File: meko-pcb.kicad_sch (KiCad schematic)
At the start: 5 parts, among them IC2 AS5600-ASOM, J1 FH34SRJ-24S-0.5SH_99_, J2 MEM2090-00-145-00-A, SW1 SW_Push, U1 ESP32-PICO-MINI-02

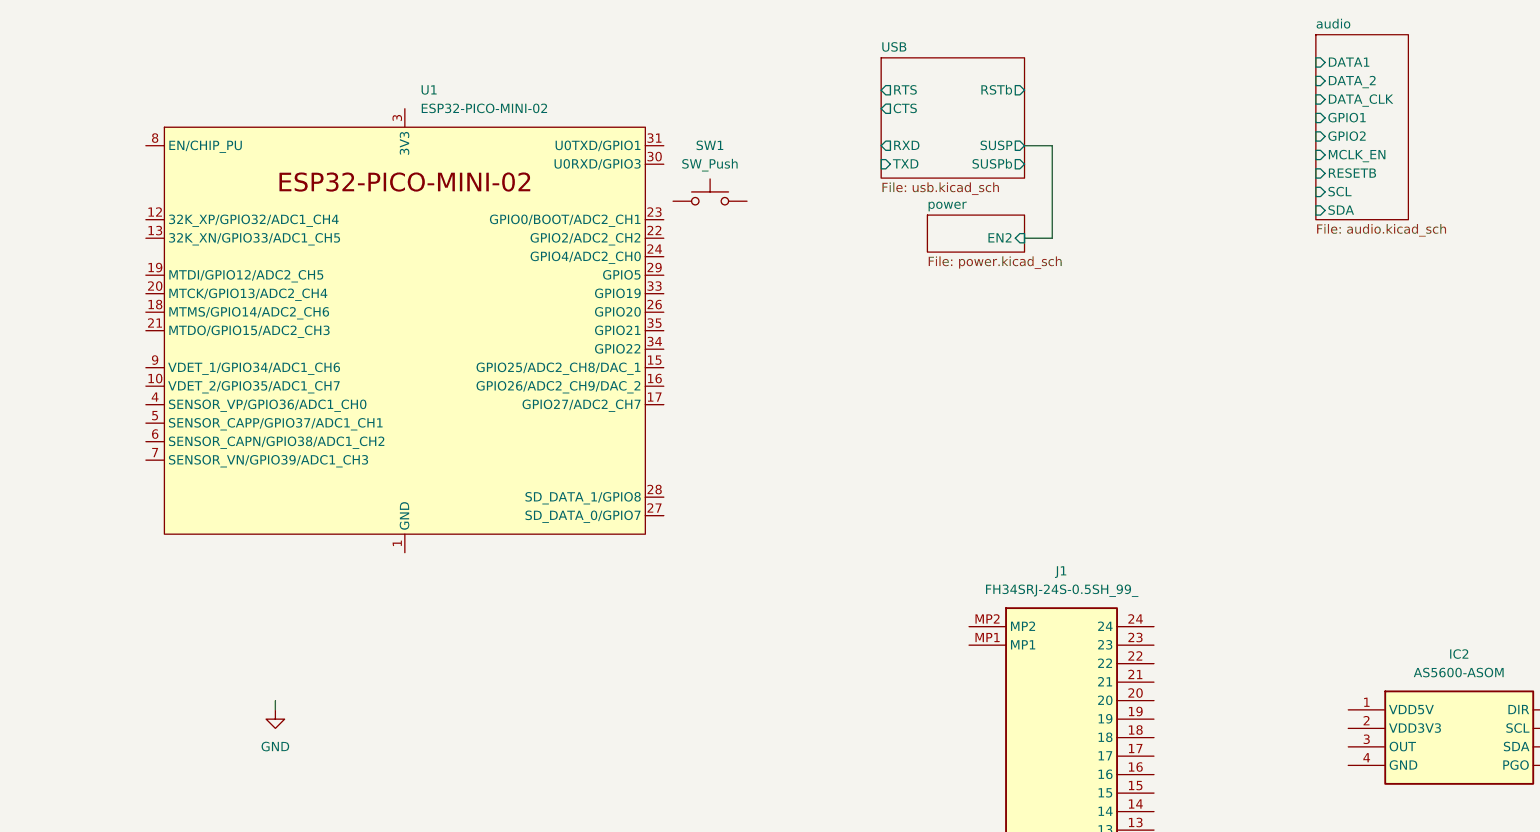
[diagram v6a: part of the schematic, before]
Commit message: made the jouranl complient, back-journaled
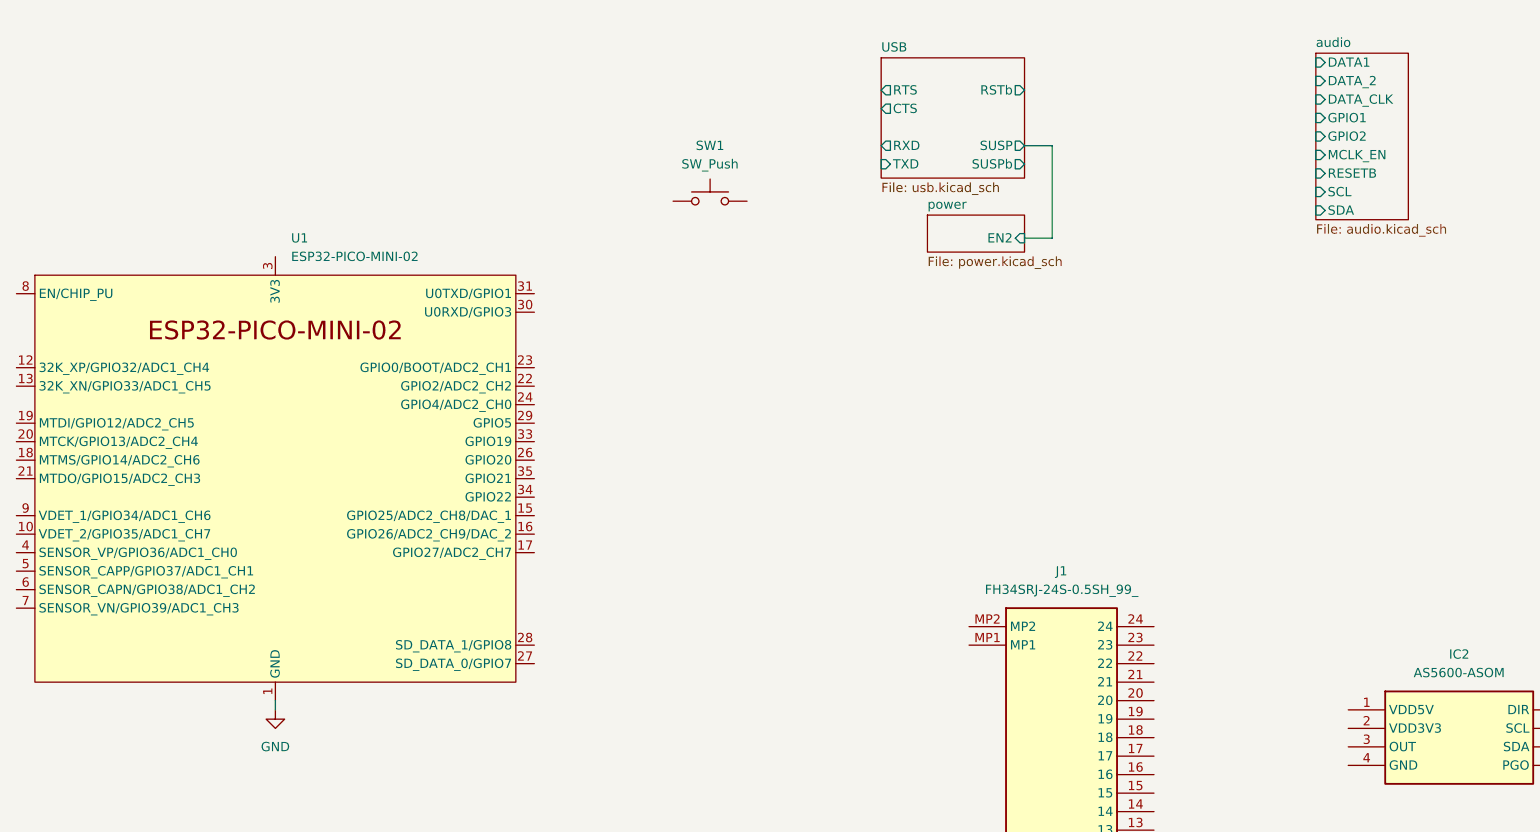
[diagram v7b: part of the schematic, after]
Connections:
- net GND: now also U1.1 (GND), U1.11 (GND), U1.14 (GND), U1.2 (GND), U1.36 (GND), U1.37 (GND), U1.38 (GND), U1.39 (GND), U1.40 (GND), U1.41 (GND), U1.42 (GND), U1.43 (GND), U1.44 (GND), U1.45 (GND), U1.46 (GND), U1.47 (GND), U1.48 (GND), U1.49 (GND), U1.50 (GND), U1.51 (GND), U1.52 (GND), U1.53 (GND)
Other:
- moved on the sheet: U1
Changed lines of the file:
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@@
 	(symbol
 		(lib_id "PCM_Espressif:ESP32-PICO-MINI-02")
-		(at 102.87 63.5 0)
+		(at 85.09 83.82 0)
 		(unit 1)
 		(exclude_from_sim no)
@@
 		(fields_autoplaced yes)
 		(property "Reference" "U1"
-			(at 105.0133 30.48 0)
+			(at 87.2333 50.8 0)
 			(effects
 				(font
@@
 		)
 		(property "Value" "ESP32-PICO-MINI-02"
-			(at 105.0133 33.02 0)
+			(at 87.2333 53.34 0)
 			(effects
 				(font
@@
 		)
 		(property "Footprint" "PCM_Espressif:ESP32-PICO-MINI-02"
-			(at 102.87 107.95 0)
+			(at 85.09 128.27 0)
 			(effects
 				(font
@@
 		)
 		(property "Datasheet" "https://www.espressif.com/sites/default/files/documentation/esp32-pico-mini-02_datasheet_en.pdf"
-			(at 102.87 110.49 0)
+			(at 85.09 130.81 0)
 			(effects
 				(font
@@
 		)
 		(property "Description" "ESP32-PICO-V3-02 MCU, SiP, 8MB Flash, 2 MB PSRAM in ESP32-MINI-format"
-			(at 102.87 63.5 0)
+			(at 85.09 83.82 0)
 			(effects
 				(font
@@
 	)
 	(sheet
-		(at 227.965 22.86)
-		(size 12.7 25.4)
+		(at 227.965 25.4)
+		(size 12.7 22.86)
 		(exclude_from_sim no)
 		(in_bom yes)
@@
 		)
 		(property "Sheetname" "audio"
-			(at 227.965 22.1484 0)
-			(effects
-				(font
+			(at 227.965 24.6884 0)
+			(effects
+				(font

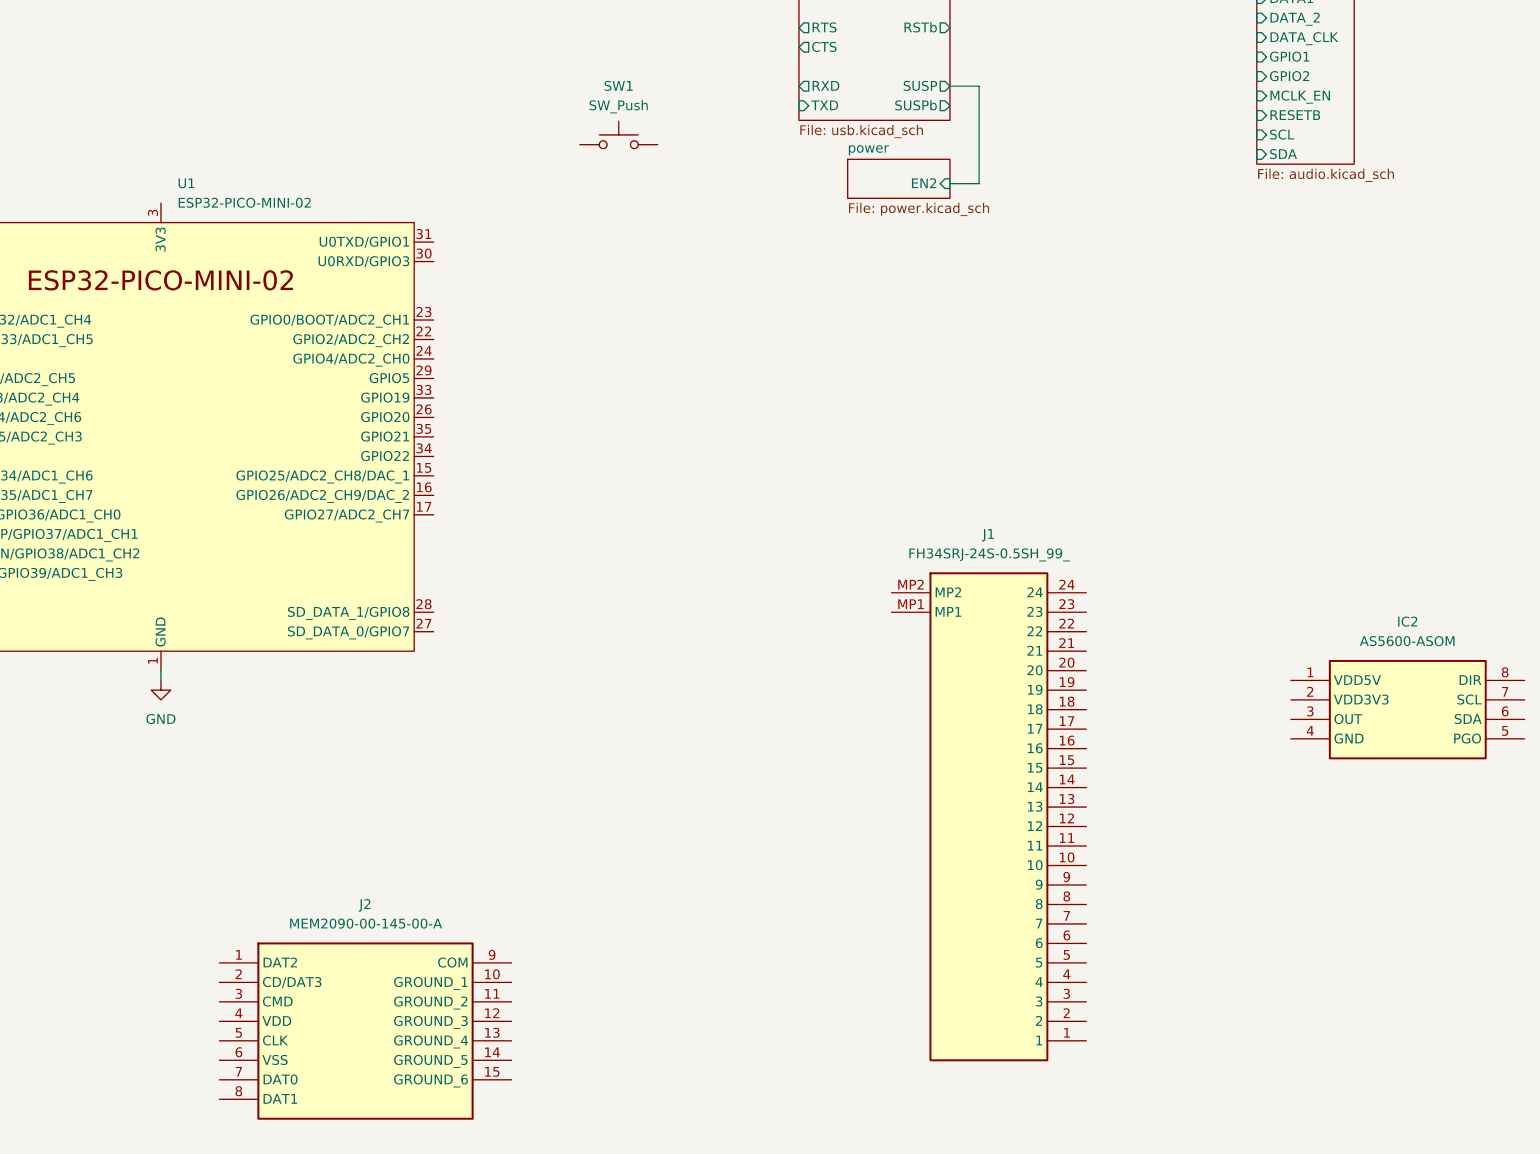
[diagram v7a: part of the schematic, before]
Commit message: re-did power with the new small LDOs and power system
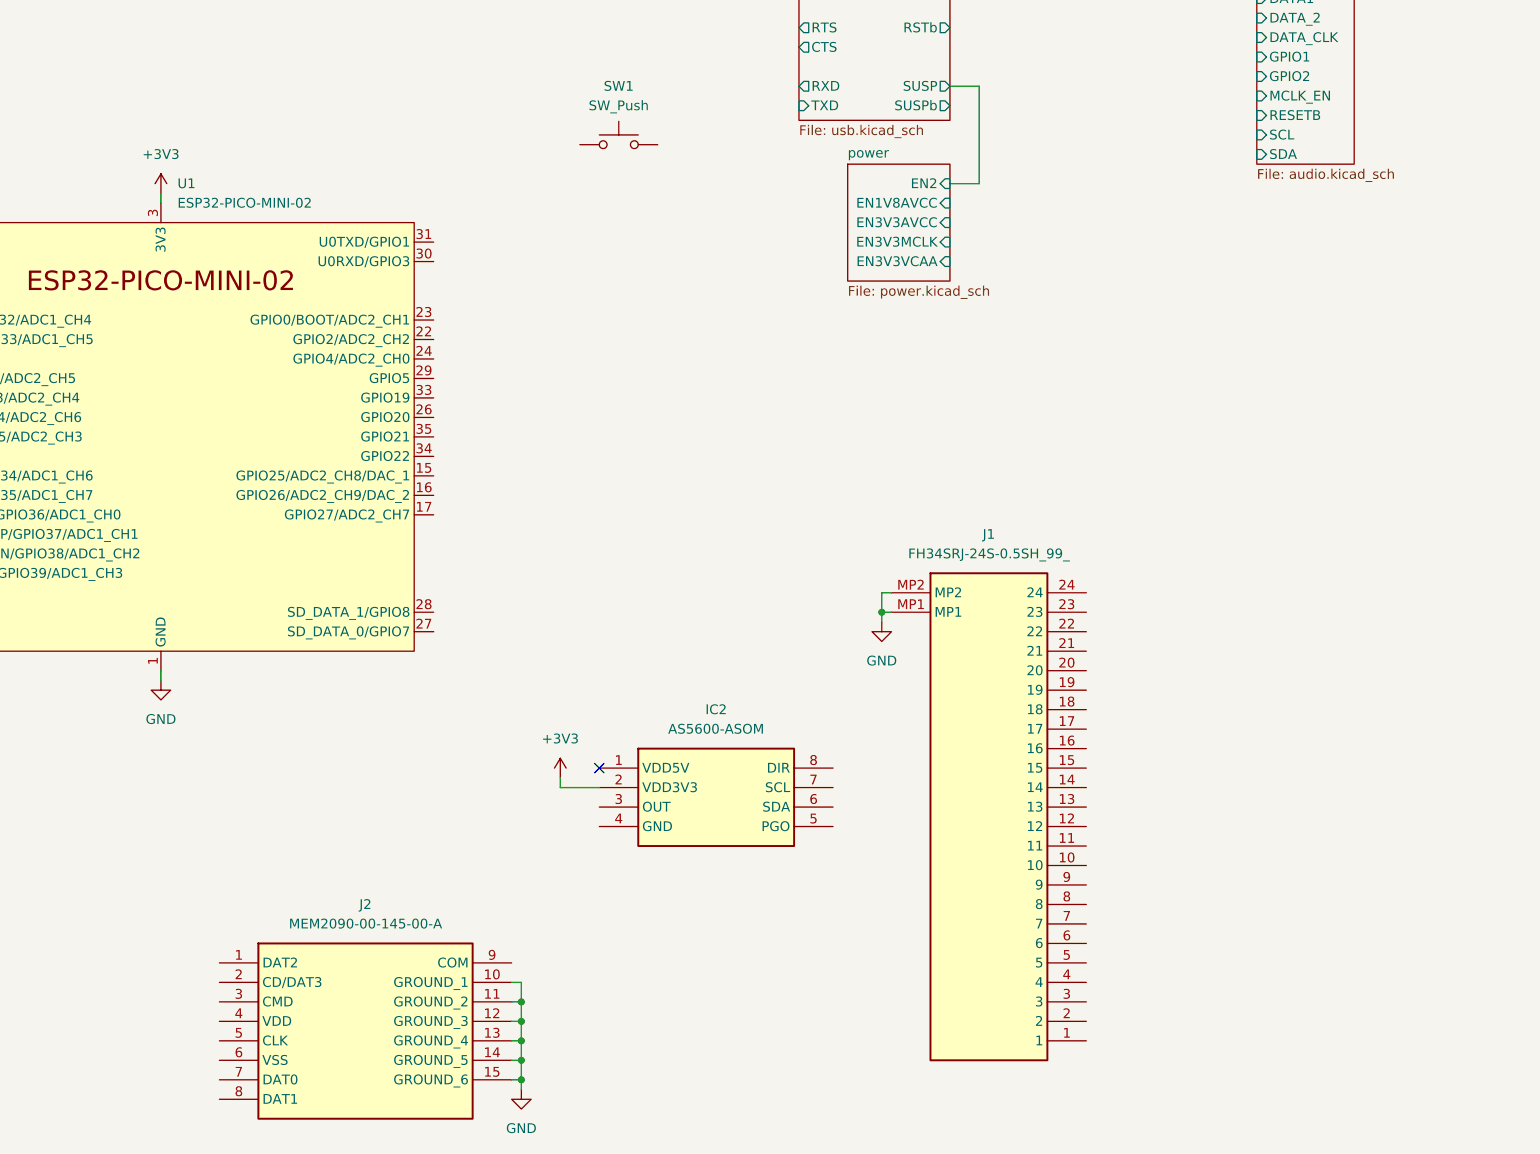
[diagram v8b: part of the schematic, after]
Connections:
- net GND: now also J1.MP1, J1.MP2, J2.10 (GROUND_1), J2.11 (GROUND_2), J2.12 (GROUND_3), J2.13 (GROUND_4), J2.14 (GROUND_5), J2.15 (GROUND_6)
- net +3V3: now reaches U1.3 (3V3)
- net +3V3: now also IC2.2 (VDD3V3)
- no-connect marks 0 -> 1
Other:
- sheet power ports: added EN1V8AVCC, EN3V3AVCC, EN3V3MCLK, EN3V3VCAA; removed none
- moved on the sheet: IC2
